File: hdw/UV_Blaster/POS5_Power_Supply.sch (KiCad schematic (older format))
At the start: 24 parts

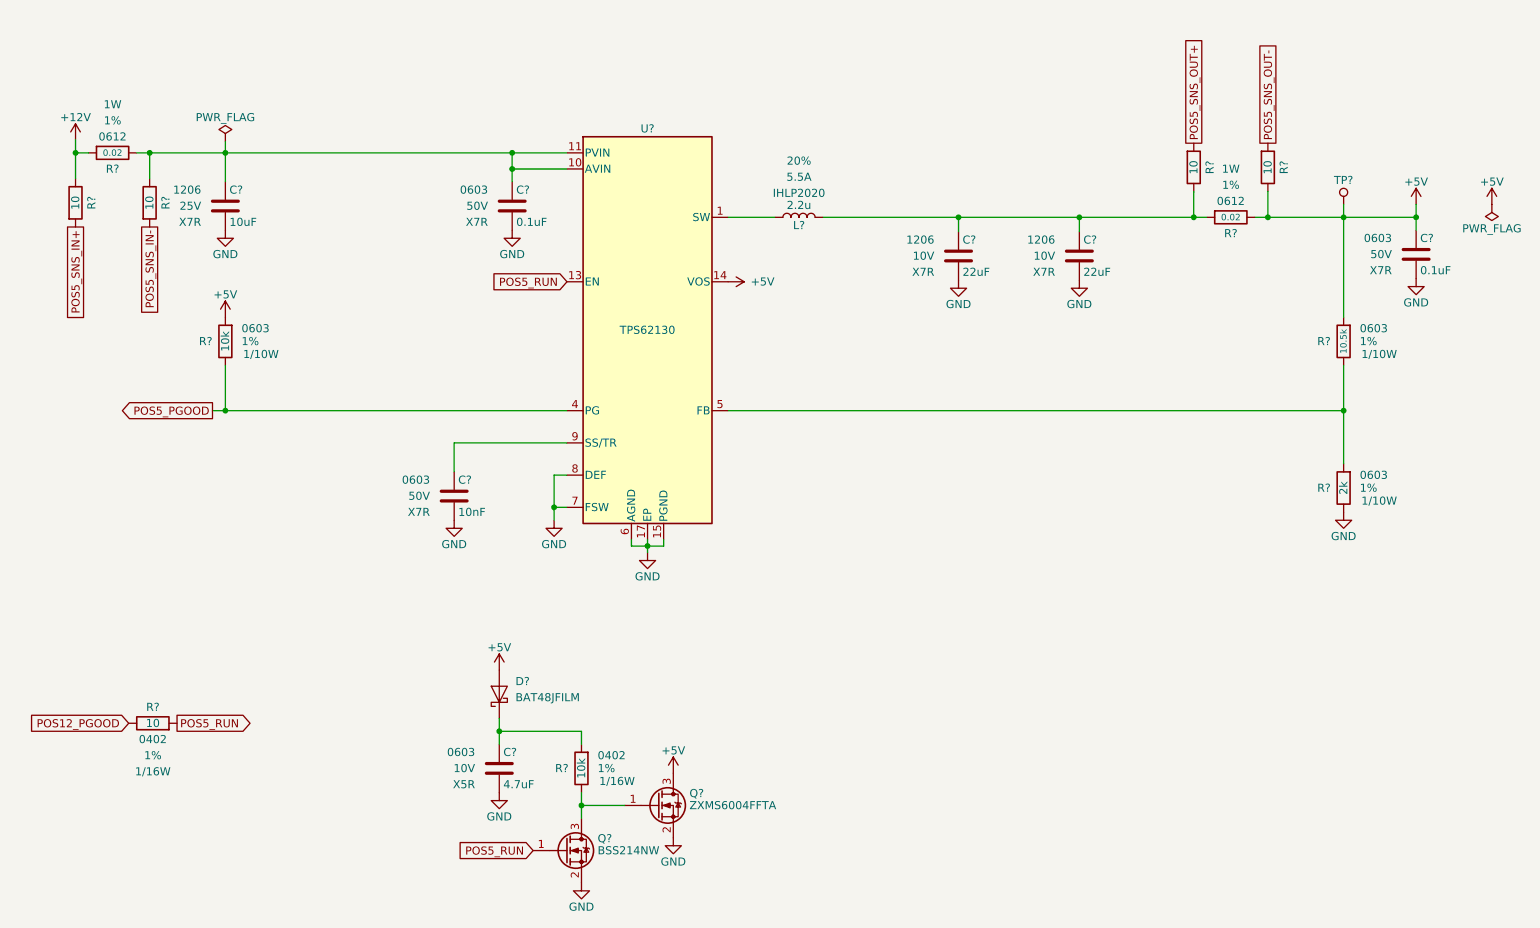
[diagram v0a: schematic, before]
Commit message: More sch work, netlist, part numbers, footprints
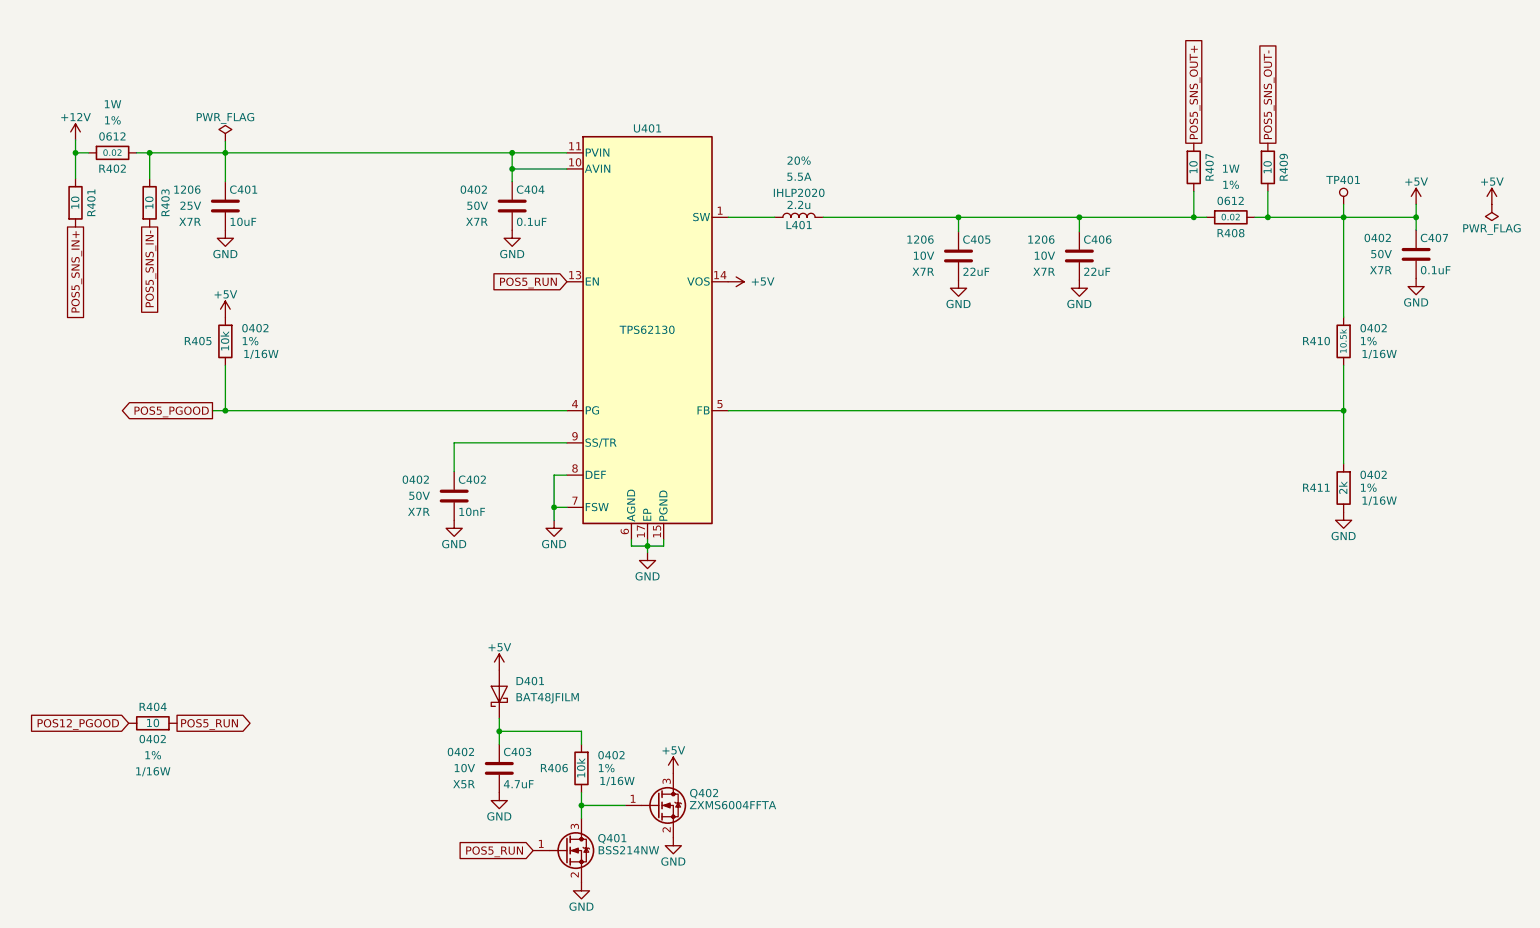
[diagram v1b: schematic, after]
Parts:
- C402: renamed from C?; footprint Capacitors_SMD:C_0603 -> Capacitors_SMD:C_0402; Digi-Key PN 1276-1921-1-ND -> 490-13295-1-ND; display_footprint 0603 -> 0402
- C403: renamed from C?; footprint Capacitors_SMD:C_0603 -> Capacitors_SMD:C_0402; Digi-Key PN 490-16348-1-ND -> 490-14306-1-ND; display_footprint 0603 -> 0402
- C404, C407: renamed from C?; footprint Capacitors_SMD:C_0603 -> Capacitors_SMD:C_0402; Digi-Key PN 490-8020-1-ND -> 490-10701-1-ND; display_footprint 0603 -> 0402
- D401: renamed from D?; Digi-Key PN (none) -> 497-5711-1-ND
- R401, R403, R407, R409: renamed from R?; Configuration (none) -> Telemetry; Digi-Key PN (none) -> 311-10.0LRCT-ND
- R404: renamed from R?; Digi-Key PN (none) -> 311-10.0LRCT-ND
- R405: renamed from R?; footprint Resistors_SMD:R_0603 -> Resistors_SMD:R_0402; Digi-Key PN RHM10KADCT-ND -> 541-3959-1-ND; Wattage 1/10W -> 1/16W; display_footprint 0603 -> 0402
- R406: renamed from R?; Digi-Key PN (none) -> 541-3959-1-ND
- R410: renamed from R?; footprint Resistors_SMD:R_0603 -> Resistors_SMD:R_0402; Digi-Key PN 311-10.5KHRCT-ND -> RMCF0402FT10K5CT-ND; Wattage 1/10W -> 1/16W; display_footprint 0603 -> 0402
- R411: renamed from R?; footprint Resistors_SMD:R_0603 -> Resistors_SMD:R_0402; Digi-Key PN 311-2.00KHRCT-ND -> 311-2KLRCT-ND; Wattage 1/10W -> 1/16W; display_footprint 0603 -> 0402
- gave numbers to parts that had none: 10
